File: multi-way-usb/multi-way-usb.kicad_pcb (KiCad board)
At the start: 2 copper layers, 92 x 92 mm, 60 parts, among them J1 USB_A, J10 USB_A, J11 USB_A, J12 USB_A, J13 USB_A, J14 USB_A, J15 USB_A, J16 USB_A, J17 USB_A, J18 USB_A, J19 USB_A, J2 USB_A, J20 USB_A, J21 USB_A, J22 USB_A, J23 USB_A, J24 USB_A, J25 USB_B_Micro, J26 USB_B_Micro, J27 Conn_01x02, J28 Conn_01x02, J3 USB_A, J4 USB_A, J5 USB_A, J6 USB_A, J7 USB_A, J8 USB_A, J9 USB_A

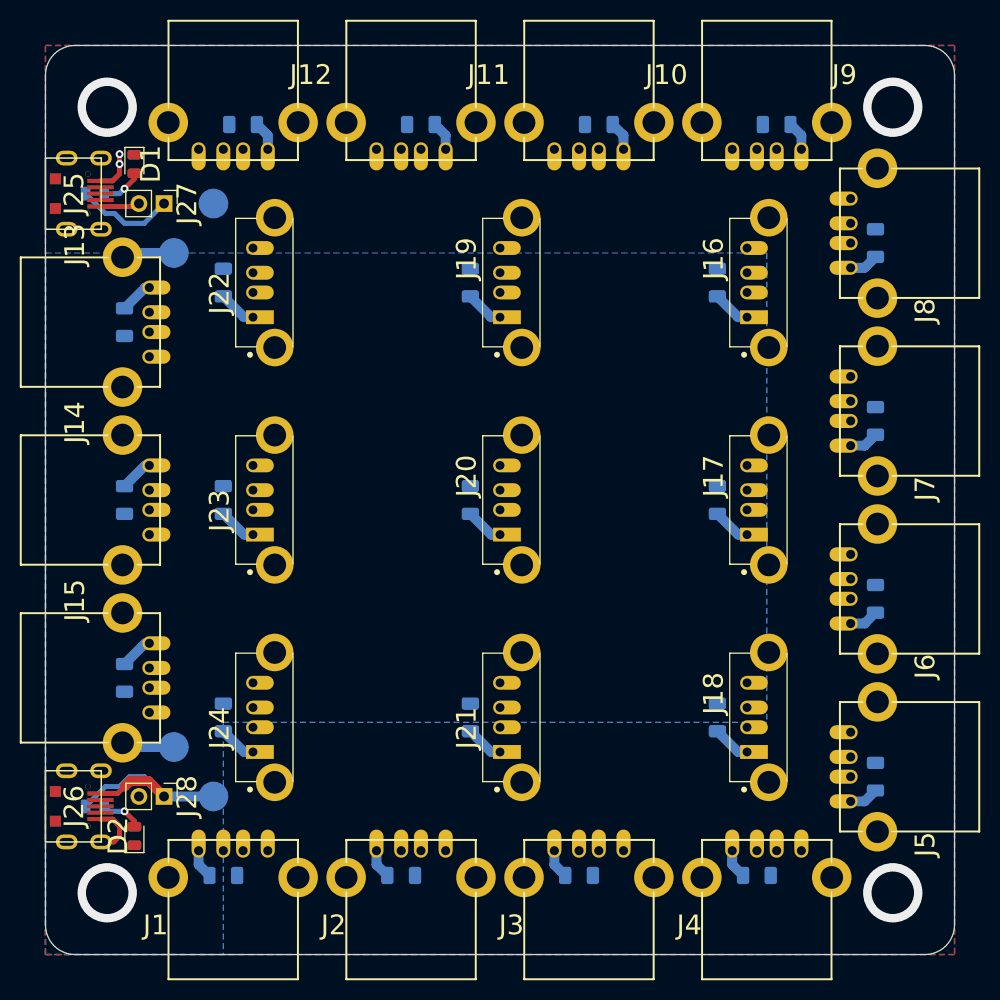
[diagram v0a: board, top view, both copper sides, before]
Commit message: multi-way-usb: Changed footprint for inverted connectors
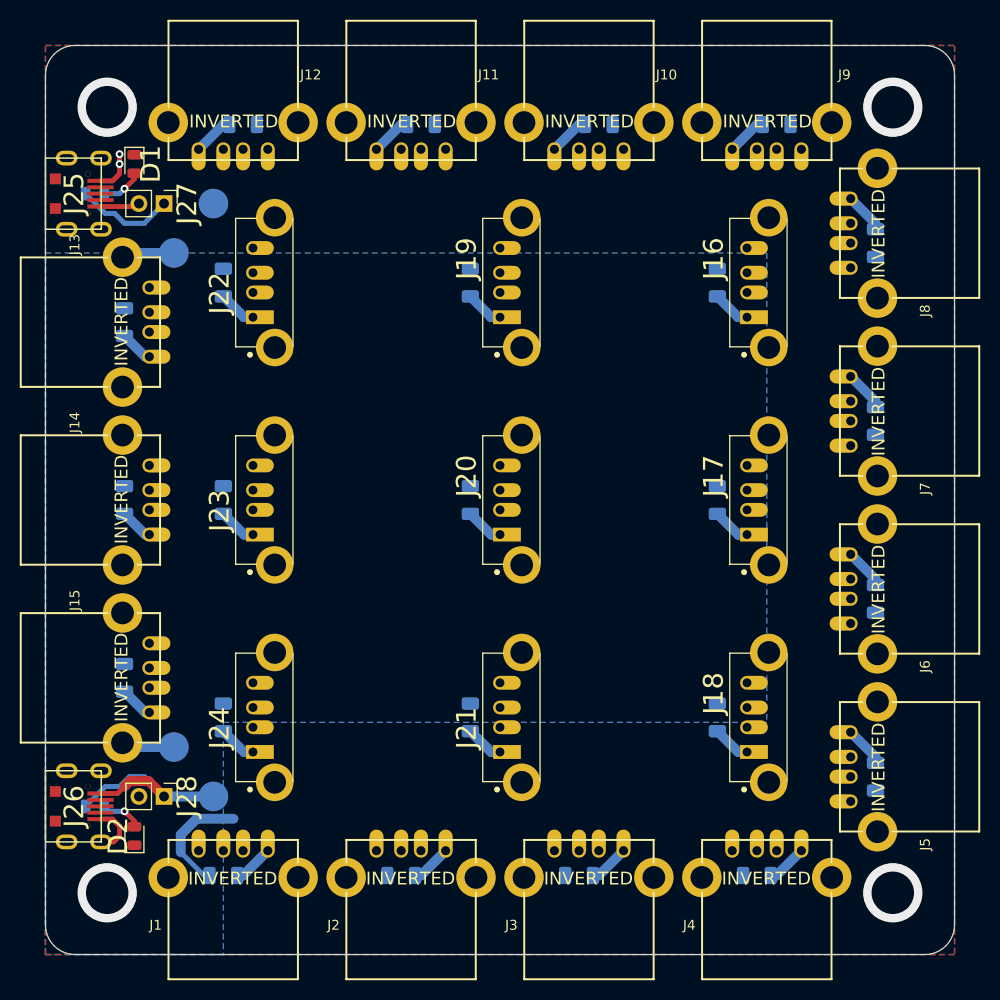
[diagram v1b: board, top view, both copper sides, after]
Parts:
- J1, J10, J11, J12, J13, J14, J15, J2, J3, J4, J5, J6, J7, J8, J9: footprint tom-connectors:OST_USB-A1HSW6 -> tom-connectors:OST_USB-A1HSW6-INVERTED
- turned F1 to 180 degrees
- turned F10 to 0 degrees
- turned F11 to 0 degrees
- turned F12 to 0 degrees
- turned F13 to 90 degrees
- turned F14 to 90 degrees
- turned F15 to 90 degrees
- turned F2 to 180 degrees
- turned F3 to 180 degrees
- turned F4 to 180 degrees
- turned F5 to 270 degrees
- turned F6 to 270 degrees
- turned F7 to 270 degrees
- turned F8 to 270 degrees
- turned F9 to 0 degrees
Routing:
- net +5V: track 14.2 -> 25.3 mm
- net Net-(F9-Pad1): track 2.97 -> 4.14 mm
- net Net-(F8-Pad1): track 2.97 -> 4.14 mm
- net Net-(F7-Pad1): track 2.97 -> 4.14 mm
- net Net-(F6-Pad1): track 2.97 -> 4.14 mm
- net Net-(F5-Pad1): track 2.97 -> 4.14 mm
- net Net-(F4-Pad1): track 2.97 -> 4.14 mm
- net Net-(F3-Pad1): track 2.97 -> 4.14 mm
- net Net-(F2-Pad1): track 2.97 -> 4.14 mm
- net Net-(F12-Pad1): track 2.97 -> 4.14 mm
- net Net-(F11-Pad1): track 2.97 -> 4.14 mm
- net Net-(F10-Pad1): track 2.97 -> 4.14 mm
- net Net-(F1-Pad1): track 2.97 -> 4.14 mm
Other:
- board text added: "24 way usb charger 100mA per port October 2020 rev 1.1"

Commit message: multi-way-usb: fix mechanical issues
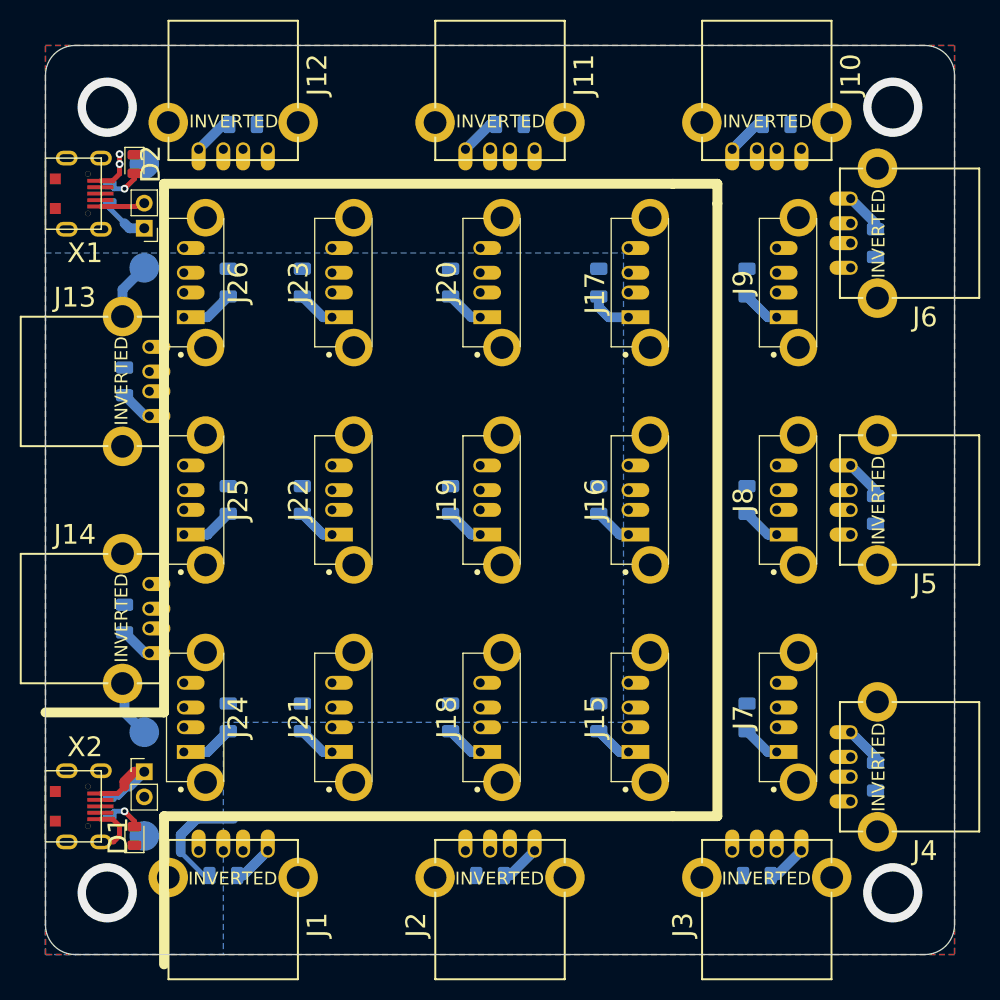
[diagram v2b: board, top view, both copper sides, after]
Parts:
- removed the J25 at (-46.0, -31.0)
- removed the R1 at (-41.0, -31.0)
- added F15: 100mA/250mA, tom-passives:C_1206_3216Metric, B.Cu at (10.0, 22.0)
- added F16: 100mA/250mA, tom-passives:C_1206_3216Metric, B.Cu at (10.0, 0.00)
- added J15: USB_A, tom-connectors:CUI_UJ2-AV-1-TH, F.Cu at (13.0, 22.0)
- added J16: USB_A, tom-connectors:CUI_UJ2-AV-1-TH, F.Cu at (13.0, 0.00)
- added R2: 1K, tom-passives:C_0805_2012Metric, B.Cu at (-39.5, -31.0)
- added X1: USB_B_Micro, tom-connectors:USB_MICRO_TAOBAO_SMD_PTH, F.Cu at (-46.0, -31.0)
- J17: renamed from J14; footprint tom-connectors:OST_USB-A1HSW6-INVERTED -> tom-connectors:CUI_UJ2-AV-1-TH
- J7: renamed from J3; footprint tom-connectors:OST_USB-A1HSW6-INVERTED -> tom-connectors:CUI_UJ2-AV-1-TH
- J8: renamed from J6; footprint tom-connectors:OST_USB-A1HSW6-INVERTED -> tom-connectors:CUI_UJ2-AV-1-TH
- J9: renamed from J10; footprint tom-connectors:OST_USB-A1HSW6-INVERTED -> tom-connectors:CUI_UJ2-AV-1-TH
- moved J17 59.2 mm to (13.0, -22.0), turned to 90 degrees
- moved F17 52.8 mm to (10.0, -22.0)
- moved J7 27.6 mm to (28.0, 22.0), turned to 90 degrees
- moved J9 27.6 mm to (28.0, -22.0), turned to 90 degrees
- moved F18 27.0 mm to (-5.00, 22.0)
- moved F19 27.0 mm to (-5.00, 0.00)
- moved F20 27.0 mm to (-5.00, -22.0)
- moved J18 27.0 mm to (-2.00, 22.0)
- moved J19 27.0 mm to (-2.00, 0.00)
- moved J20 27.0 mm to (-2.00, -22.0)
- moved F7 23.3 mm to (25.0, 22.0), turned to 90 degrees
- moved F9 21.9 mm to (25.0, -22.0), turned to 90 degrees
- moved F21 17.0 mm to (-20.0, 22.0)
- moved F22 17.0 mm to (-20.0, 0.00)
- moved F23 17.0 mm to (-20.0, -22.0)
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- renumbered D2 to D1, D1 to D2, F9 to F10, F15 to F14, F14 to F17, F17 to F19, F16 to F20, F20 to F22, F19 to F23, F23 to F25, F22 to F26, F4 to F3, F5 to F4, F7 to F5, F8 to F6, F3 to F7, F6 to F8, F10 to F9, J9 to J10, J15 to J14, J17 to J19, J16 to J20, J20 to J22, J19 to J23, J23 to J25, J22 to J26, J4 to J3, J5 to J4, J7 to J5, J8 to J6, R2 to R1, J26 to X2, J27 to X3, J28 to X4
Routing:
- net +5VA: track 22.6 -> 10.2 mm
- net +5V: track 25.3 -> 20.2 mm
- net Net-(F15-Pad1): track 0.00 -> 3.87 mm
- net Net-(F16-Pad1): track 0.00 -> 3.87 mm
- net GND: track 20.1 -> 22.3 mm
- net Net-(F25-Pad1): track 3.87 -> 5.37 mm
- net Net-(F26-Pad1): track 3.87 -> 5.37 mm
- net Net-(F24-Pad1): track 3.87 -> 5.37 mm
- net Net-(F17-Pad1): track 3.38 -> 4.51 mm
- net Net-(D2-Pad2): track 4.25 -> 3.66 mm
- net Net-(D1-Pad2): track 4.25 -> 3.66 mm
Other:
- board text added: "November 2020 rev 1.2"
- board text removed: "24 way usb charger 100mA per port October 2020 rev 1.1"

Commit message: multi-way-usb: move J8 to X2 to balance supplies, v1.2 ready for production
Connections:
- F8 pad 2: +5V -> +5VA
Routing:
- net +5VA: track 10.2 -> 33.1 mm, vias 0 -> 2
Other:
- rule pad_to_mask_clearance: 0.05 -> 0
